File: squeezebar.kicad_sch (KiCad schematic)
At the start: 43 parts, among them J1 RESET, J2 Conn_02x08_Counter_Clockwise, J3 I2C, U1 Elite-C

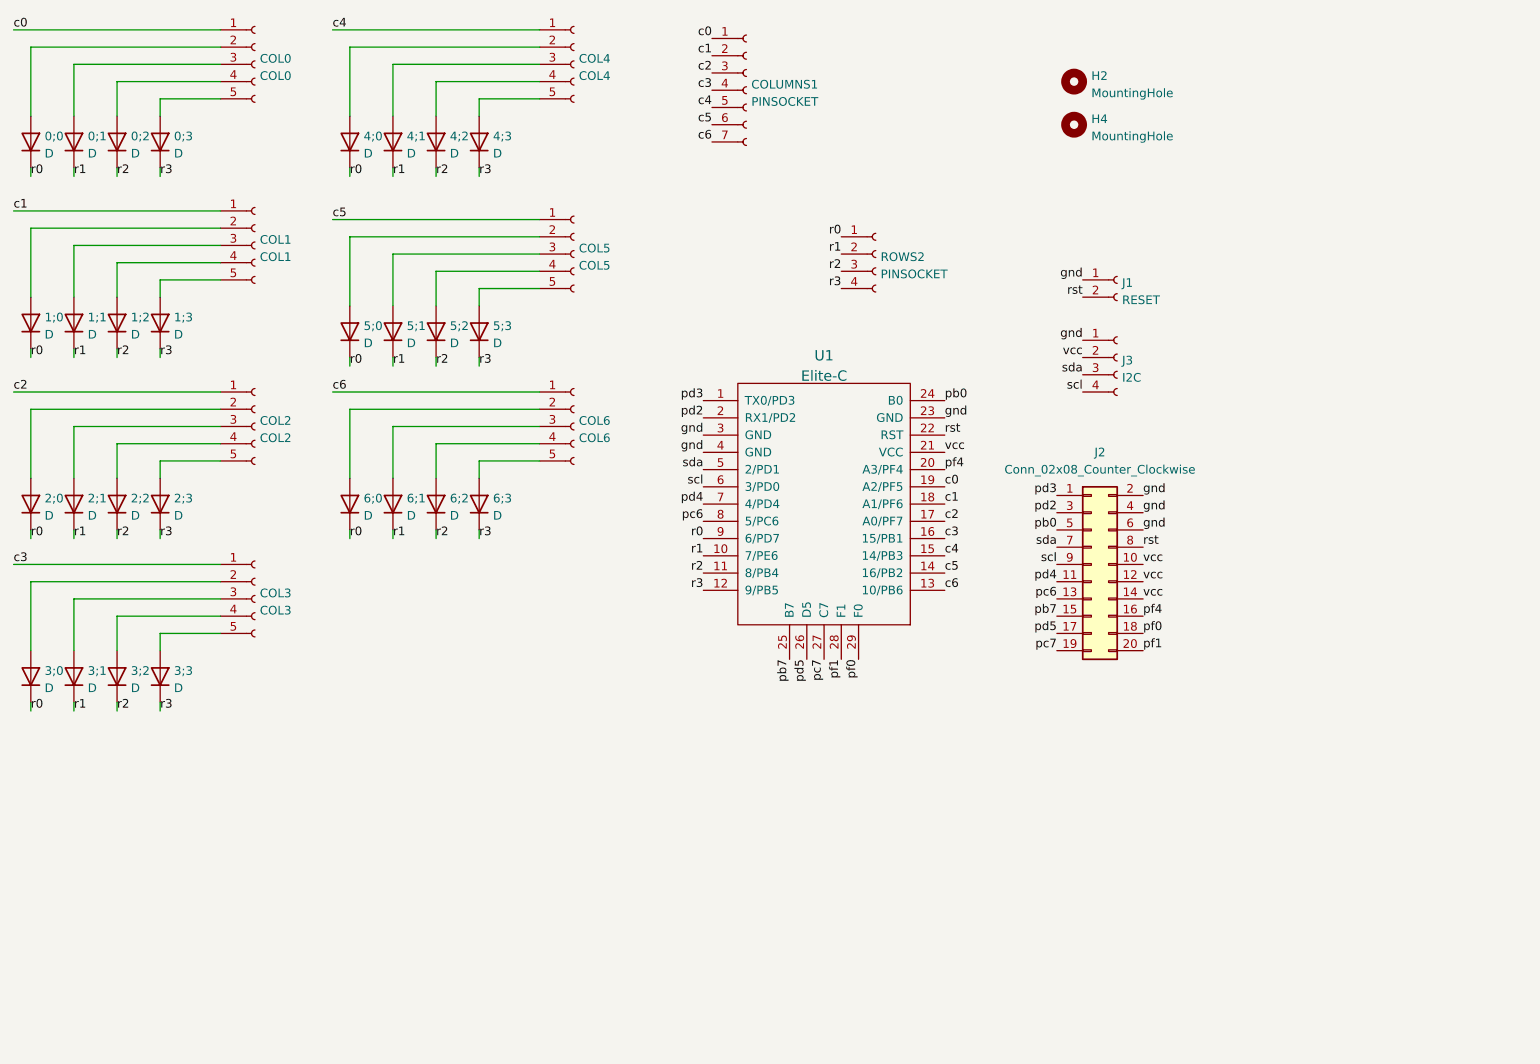
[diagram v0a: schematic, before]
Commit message: Squeezebar: Make it passive, with JST connectors
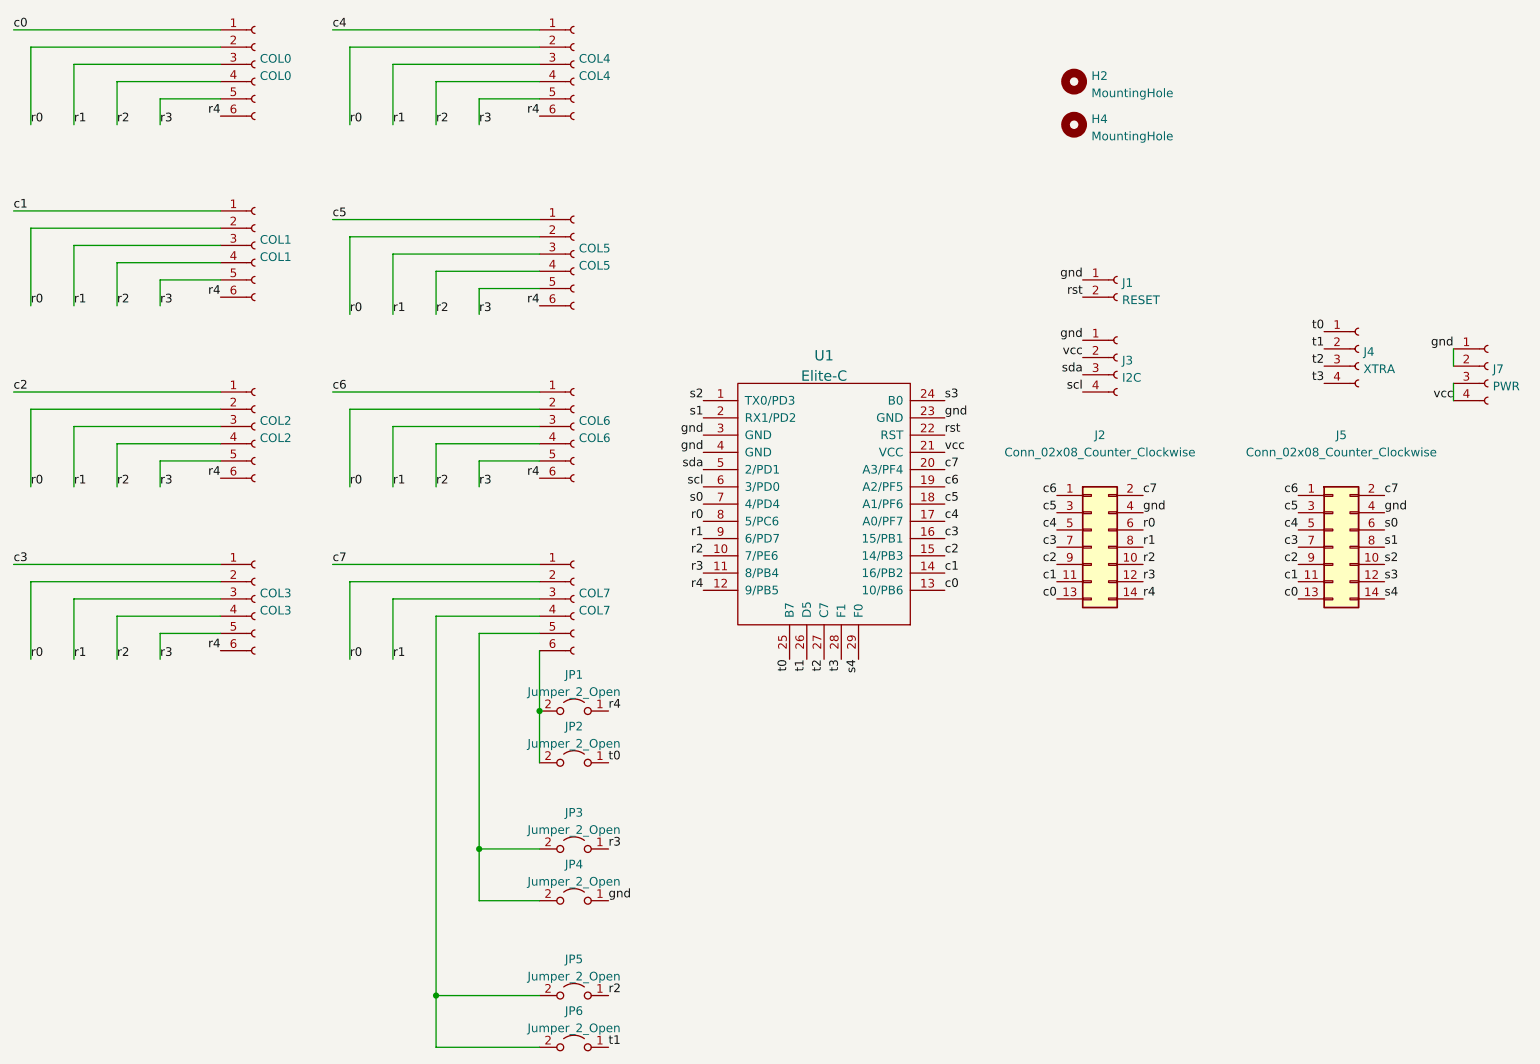
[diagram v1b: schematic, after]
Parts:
- removed 0;0, 0;1, 0;2, 0;3, 1;0, 1;1, 1;2, 1;3, 2;0, 2;1, 2;2, 2;3, 3;0, 3;1, 3;2, 3;3, 4;0, 4;1, 4;2, 4;3, 5;0, 5;1, 5;2, 5;3, 6;0, 6;1, 6;2, 6;3: D, Library:Diode, symbol Device:D
- removed COLUMNS1: PINSOCKET, Library:PinHeader_COLS_1x07_P2.54mm_Vertical, symbol Connector:Conn_01x07_Female
- removed ROWS2: PINSOCKET, Library:PinSocket_1x04_P2.54mm_Vertical_LongPads, symbol Connector:Conn_01x04_Female
- added COL7: COL7, Connector_JST:JST_XH_B6B-XH-A_1x06_P2.50mm_Vertical, symbol Connector:Conn_01x06_Female
- added J4: XTRA, Connector_PinHeader_2.54mm:PinHeader_1x04_P2.54mm_Vertical, symbol Connector:Conn_01x04_Female
- added J5: Conn_02x08_Counter_Clockwise, Connector_IDC:IDC-Header_2x07_P2.54mm_Vertical, symbol Connector_Generic:Conn_02x07_Odd_Even
- added J7: PWR, Connector_PinHeader_2.54mm:PinHeader_1x04_P2.54mm_Vertical, symbol Connector:Conn_01x04_Female
- added JP1, JP2, JP3, JP4, JP5, JP6: Jumper_2_Open, Jumper:SolderJumper-2_P1.3mm_Open_TrianglePad1.0x1.5mm, symbol Jumper:Jumper_2_Open
- COL0, COL1, COL2, COL3, COL4, COL5, COL6: footprint Library:PinHeader_Col_1x05_P2.54mm_Vertical -> Connector_JST:JST_XH_B6B-XH-A_1x06_P2.50mm_Vertical; symbol Connector:Conn_01x05_Female -> Connector:Conn_01x06_Female
- J1: footprint Library:PinHeader_RST_1x02_P2.54mm_Vertical -> Connector_JST:JST_XH_B2B-XH-A_1x02_P2.50mm_Vertical
- J2: footprint Connector_PinSocket_2.54mm:PinSocket_2x10_P2.54mm_Vertical -> Connector_IDC:IDC-Header_2x07_P2.54mm_Vertical; symbol Connector_Generic:Conn_02x10_Odd_Even -> Connector_Generic:Conn_02x07_Odd_Even
- J3: footprint Library:PinHeader_I2C_1x04_P2.54mm_Vertical -> Connector_JST:JST_XH_B4B-XH-A_1x04_P2.50mm_Vertical
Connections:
- net c0: now also J2.13 (Pin_13), U1.13 (10/PB6), J5.13 (Pin_13); no longer U1.19 (A2/PF5)
- net c1: now also J2.11 (Pin_11), U1.14 (16/PB2), J5.11 (Pin_11); no longer U1.18 (A1/PF6)
- net c2: now also J2.9 (Pin_9), U1.15 (14/PB3), J5.9 (Pin_9); no longer U1.17 (A0/PF7)
- net c3: now also J2.7 (Pin_7), J5.7 (Pin_7)
- net c4: now also J2.5 (Pin_5), U1.17 (A0/PF7), J5.5 (Pin_5); no longer U1.15 (14/PB3)
- net c5: now also J2.3 (Pin_3), U1.18 (A1/PF6), J5.3 (Pin_3); no longer U1.14 (16/PB2)
- net c6: now also J2.1 (Pin_1), U1.19 (A2/PF5), J5.1 (Pin_1); no longer U1.13 (10/PB6)
- net gnd: now also J5.4 (Pin_4), J7.1 (Pin_1), J7.2 (Pin_2), JP4.1 (A); no longer J2.2 (Pin_2), J2.6 (Pin_6)
- net r0: now also COL0.2 (Pin_2), COL1.2 (Pin_2), COL2.2 (Pin_2), COL3.2 (Pin_2), COL4.2 (Pin_2), COL5.2 (Pin_2), COL6.2 (Pin_2), J2.6 (Pin_6), U1.8 (5/PC6), COL7.2 (Pin_2); no longer U1.9 (6/PD7)
- net r1: now also COL0.3 (Pin_3), COL1.3 (Pin_3), COL2.3 (Pin_3), COL3.3 (Pin_3), COL4.3 (Pin_3), COL5.3 (Pin_3), COL6.3 (Pin_3), J2.8 (Pin_8), U1.9 (6/PD7), COL7.3 (Pin_3); no longer U1.10 (7/PE6)
- net r2: now also COL0.4 (Pin_4), COL1.4 (Pin_4), COL2.4 (Pin_4), COL3.4 (Pin_4), COL4.4 (Pin_4), COL5.4 (Pin_4), COL6.4 (Pin_4), J2.10 (Pin_10), U1.10 (7/PE6), JP5.1 (A); no longer U1.11 (8/PB4)
- net r3: now also COL0.5 (Pin_5), COL1.5 (Pin_5), COL2.5 (Pin_5), COL3.5 (Pin_5), COL4.5 (Pin_5), COL5.5 (Pin_5), COL6.5 (Pin_5), J2.12 (Pin_12), U1.11 (8/PB4), JP3.1 (A); no longer U1.12 (9/PB5)
- net rst: no longer J2.8 (Pin_8)
- net scl: no longer J2.9 (Pin_9)
- net sda: no longer J2.7 (Pin_7)
- net vcc: now also J7.3 (Pin_3), J7.4 (Pin_4); no longer J2.10 (Pin_10), J2.12 (Pin_12), J2.14 (Pin_14)
- net pb0 renamed s3
- net s3: now also J5.12 (Pin_12); no longer J2.5 (Pin_5)
- net pb7 renamed t0
- net t0: now also J4.1 (Pin_1), JP2.1 (A); no longer J2.15 (Pin_15)
- removed net pc6: J2.13 (Pin_13), U1.8 (5/PC6)
- net pc7 renamed t2
- net t2: now also J4.3 (Pin_3); no longer J2.19 (Pin_19)
- net pd2 renamed s1
- net s1: now also J5.8 (Pin_8); no longer J2.3 (Pin_3)
- net pd3 renamed s2
- net s2: now also J5.10 (Pin_10); no longer J2.1 (Pin_1)
- net pd4 renamed s0
- net s0: now also J5.6 (Pin_6); no longer J2.11 (Pin_11)
- net pd5 renamed t1
- net t1: now also J4.2 (Pin_2), JP6.1 (A); no longer J2.17 (Pin_17)
- net pf0 renamed s4
- net s4: now also J5.14 (Pin_14); no longer J2.18 (Pin_18)
- net pf1 renamed t3
- net t3: now also J4.4 (Pin_4); no longer J2.20 (Pin_20)
- net pf4 renamed c7
- net c7: now also J2.2 (Pin_2), COL7.1 (Pin_1), J5.2 (Pin_2); no longer J2.16 (Pin_16)
- new net: COL7.6 (Pin_6), JP1.2 (B), JP2.2 (B)
- new net: COL7.5 (Pin_5), JP3.2 (B), JP4.2 (B)
- new net: COL7.4 (Pin_4), JP5.2 (B), JP6.2 (B)
- new net r4: COL0.6 (Pin_6), COL1.6 (Pin_6), COL2.6 (Pin_6), COL3.6 (Pin_6), COL4.6 (Pin_6), COL5.6 (Pin_6), COL6.6 (Pin_6), J2.14 (Pin_14), JP1.1 (A), U1.12 (9/PB5)
